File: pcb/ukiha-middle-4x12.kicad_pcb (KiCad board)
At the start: 2 copper layers, 100 x 112 mm, 10 parts

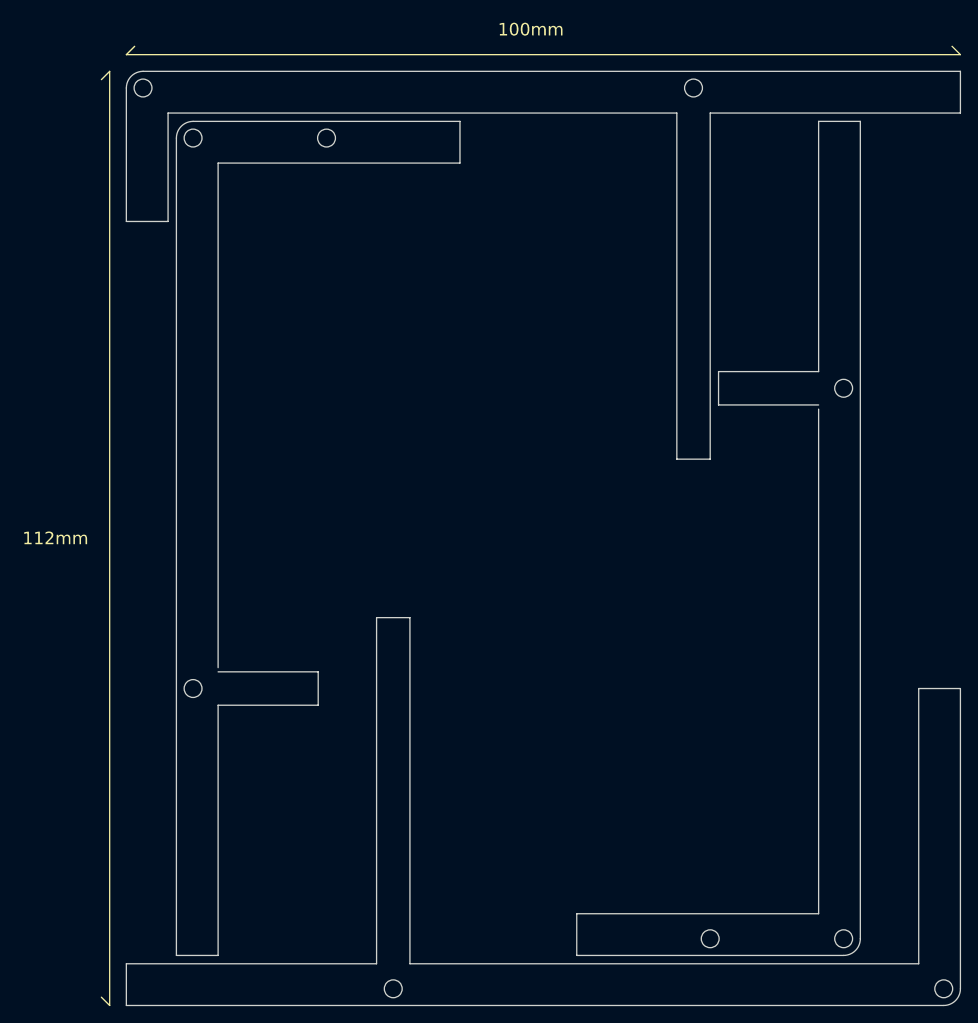
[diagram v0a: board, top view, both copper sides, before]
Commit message: Fix screw hole position
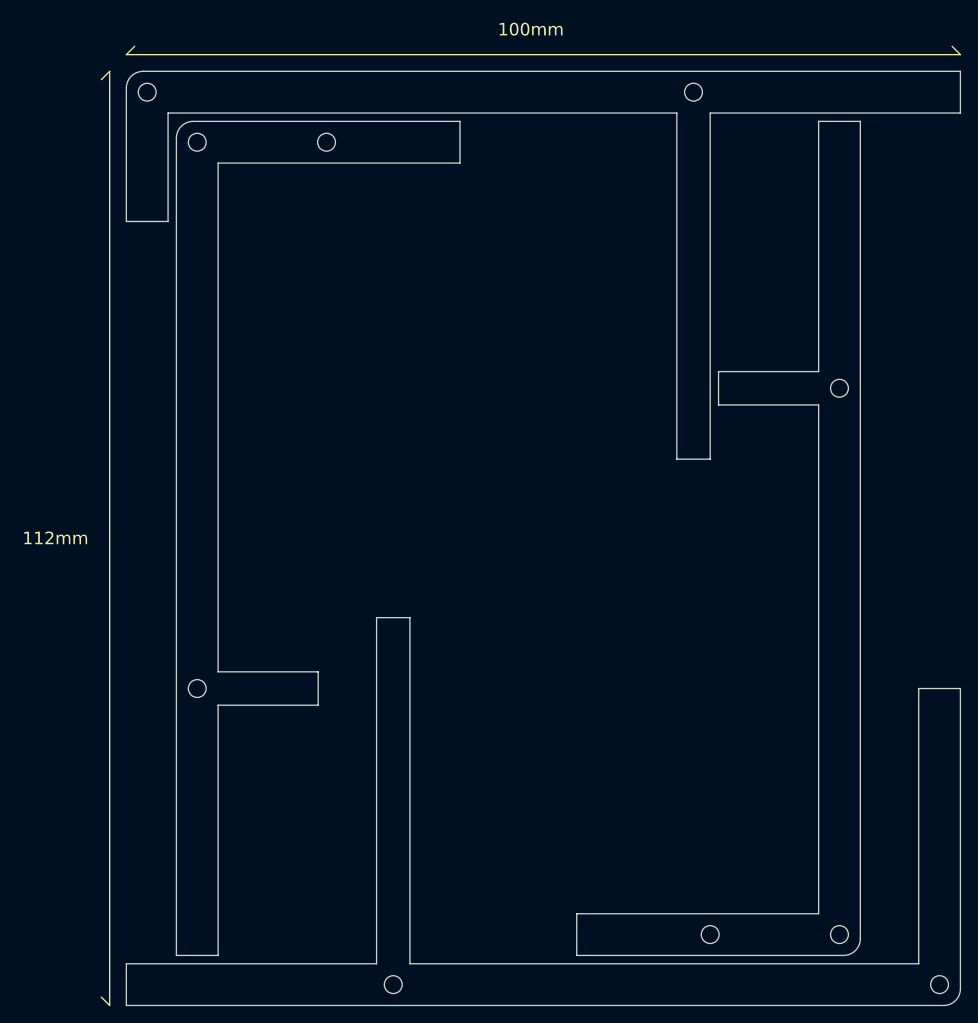
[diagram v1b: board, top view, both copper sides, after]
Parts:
- moved ? 0.71 mm to (124.6, 146.3)
- moved ? 0.71 mm to (35.6, 45.3)
- moved ? 0.71 mm to (112.6, 140.3)
- moved ? 0.71 mm to (29.6, 39.3)
- moved ? 0.50 mm to (59.1, 146.3)
- moved ? 0.50 mm to (97.1, 140.3)
- moved ? 0.50 mm to (112.6, 74.8)
- moved ? 0.50 mm to (95.1, 39.3)
- moved ? 0.50 mm to (35.6, 110.8)
- moved ? 0.50 mm to (51.1, 45.3)
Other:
- outline, holes or cut-outs redrawn
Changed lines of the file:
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@@
     (visible_elements 7FFFFFEF)
     (pcbplotparams
-      (layerselection 0x010f0_ffffffff)
+      (layerselection 0x01020_7ffffffe)
       (usegerberextensions false)
       (usegerberattributes false)
@@
       (padsonsilk false)
       (subtractmaskfromsilk true)
-      (outputformat 5)
+      (outputformat 4)
       (mirror false)
       (drillshape 0)
@@
   )
   (module "#footprint:M2_Hole_Edge.Cuts" (layer F.Cu)
-    (at 125.102501 146.80625 180)
+    (at 124.602501 146.30625 180)
     (descr "Resitance 3 pas")
     (tags R)
@@
   )
   (module "#footprint:M2_Hole_Edge.Cuts" (layer F.Cu)
-    (at 59.102501 146.80625 180)
+    (at 59.102501 146.30625 180)
     (descr "Resitance 3 pas")
     (tags R)
@@
   )
   (module "#footprint:M2_Hole_Edge.Cuts" (layer F.Cu)
-    (at 113.102501 140.80625 90)
+    (at 112.602501 140.30625 90)
     (descr "Resitance 3 pas")
     (tags R)
@@
   )
   (module "#footprint:M2_Hole_Edge.Cuts" (layer F.Cu)
-    (at 97.102501 140.80625 90)
+    (at 97.102501 140.30625 90)
     (descr "Resitance 3 pas")
     (tags R)
@@
   )
   (module "#footprint:M2_Hole_Edge.Cuts" (layer F.Cu)
-    (at 113.102501 74.80625 90)
+    (at 112.602501 74.80625 90)
     (descr "Resitance 3 pas")
     (tags R)
@@
   )
   (module "#footprint:M2_Hole_Edge.Cuts" (layer F.Cu)
-    (at 29.102501 38.80625)
+    (at 29.602501 39.30625)
     (descr "Resitance 3 pas")
     (tags R)
@@
   )
   (module "#footprint:M2_Hole_Edge.Cuts" (layer F.Cu)
-    (at 95.102501 38.80625)
+    (at 95.102501 39.30625)
     (descr "Resitance 3 pas")
     (tags R)
@@
   )
   (module "#footprint:M2_Hole_Edge.Cuts" (layer F.Cu)
-    (at 35.102501 110.80625 270)
+    (at 35.602501 110.80625 270)
     (descr "Resitance 3 pas")
     (tags R)
@@
   )
   (module "#footprint:M2_Hole_Edge.Cuts" (layer F.Cu)
-    (at 51.102501 44.80625 270)
+    (at 51.102501 45.30625 270)
     (descr "Resitance 3 pas")
     (tags R)
@@
   )
   (module "#footprint:M2_Hole_Edge.Cuts" (layer F.Cu)
-    (at 35.102501 44.80625 270)
+    (at 35.602501 45.30625 270)
     (descr "Resitance 3 pas")
     (tags R)
@@
   (gr_line (start 115.102501 42.80625) (end 115.102501 140.80625) (layer Edge.Cuts) (width 0.15))
   (gr_line (start 98.102501 72.80625) (end 110.102501 72.80625) (layer Edge.Cuts) (width 0.15))
-  (gr_line (start 110.102501 137.80625) (end 110.102501 77.30625) (layer Edge.Cuts) (width 0.15))
+  (gr_line (start 110.102501 137.80625) (end 110.102501 76.80625) (layer Edge.Cuts) (width 0.15))
   (gr_line (start 97.102501 83.30625) (end 93.102501 83.30625) (layer Edge.Cuts) (width 0.15))
   (gr_line (start 32.102501 41.80625) (end 32.102501 54.80625) (layer Edge.Cuts) (width 0.15))
@@
   (gr_line (start 67.102501 42.80625) (end 67.102501 47.80625) (layer Edge.Cuts) (width 0.15))
   (gr_line (start 67.102501 47.80625) (end 38.102501 47.80625) (layer Edge.Cuts) (width 0.15))
-  (gr_line (start 38.102501 47.80625) (end 38.102501 108.30625) (layer Edge.Cuts) (width 0.15))
+  (gr_line (start 38.102501 47.80625) (end 38.102501 108.80625) (layer Edge.Cuts) (width 0.15))
 )
